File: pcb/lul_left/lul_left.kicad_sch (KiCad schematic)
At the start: 42 parts, among them J1 JST Connector, J2 JST Connector, SW1 SW_Push, SW10 SW_Push, SW11 SW_Push, SW12 SW_Push, SW13 SW_Push, SW14 SW_Push, SW15 SW_Push, SW16 SW_Push, SW17 SW_Push, SW18 SW_Push, SW19 SW_Push, SW2 SW_Push, SW20 SW_Push, SW21 SW_Push, SW22 SW_Push, SW23 SW_Push, SW24 SW_Push, SW25 SW_Push, SW26 SW_Push, SW27 SW_Push, SW28 SW_Push, SW29 SW_Push, SW3 SW_Push, SW30 SW_Push, SW31 SW_Push, SW32 SW_Push, SW33 SW_Push, SW34 SW_Push, SW4 SW_Push, SW5 SW_Push, SW6 SW_Push, SW7 SW_Push, SW8 SW_Push, SW9 SW_Push, U1 nice_nano, U2 nice_nano

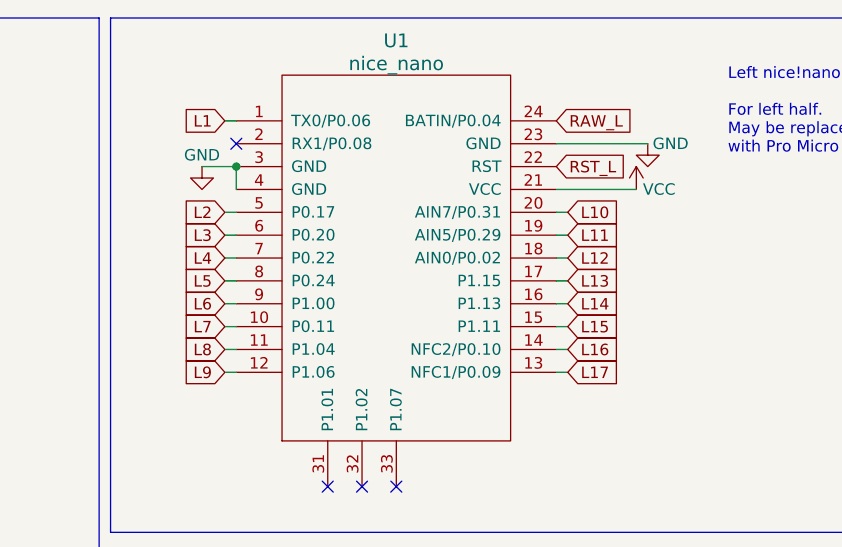
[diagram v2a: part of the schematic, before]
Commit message: route fully. Just need ground fill
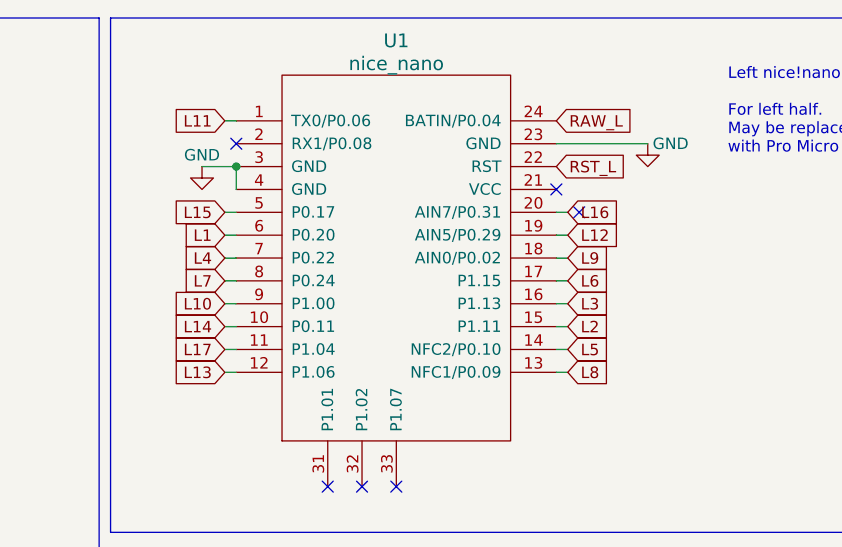
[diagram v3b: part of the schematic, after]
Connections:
- net L1: now also U1.6 (P0.20); no longer U1.1 (TX0/P0.06)
- net L10: now also U1.9 (P1.00); no longer U1.20 (AIN7/P0.31)
- net L11: now also U1.1 (TX0/P0.06); no longer U1.19 (AIN5/P0.29)
- net L12: now also U1.19 (AIN5/P0.29); no longer U1.18 (AIN0/P0.02)
- net L13: now also U1.12 (P1.06); no longer U1.17 (P1.15)
- net L14: now also U1.10 (P0.11); no longer U1.16 (P1.13)
- net L15: now also U1.5 (P0.17); no longer U1.15 (P1.11)
- net L16: now also U1.20 (AIN7/P0.31); no longer U1.14 (NFC2/P0.10)
- net L17: now also U1.11 (P1.04); no longer U1.13 (NFC1/P0.09)
- net L2: now also U1.15 (P1.11); no longer U1.5 (P0.17)
- net L3: now also U1.16 (P1.13); no longer U1.6 (P0.20)
- net L5: now also U1.14 (NFC2/P0.10); no longer U1.8 (P0.24)
- net L6: now also U1.17 (P1.15); no longer U1.9 (P1.00)
- net L7: now also U1.8 (P0.24); no longer U1.10 (P0.11)
- net L8: now also U1.13 (NFC1/P0.09); no longer U1.11 (P1.04)
- net L9: now also U1.18 (AIN0/P0.02); no longer U1.12 (P1.06)
- net VCC: no longer U1.21 (VCC)
- no-connect marks 10 -> 12
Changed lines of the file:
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@@
   (no_connect (at 157.48 64.77))
   (no_connect (at 80.01 171.45))
+  (no_connect (at 181.61 34.29))
   (no_connect (at 161.29 137.16))
   (no_connect (at 157.48 137.16))
   (no_connect (at 161.29 64.77))
+  (no_connect (at 179.07 31.75))
   (no_connect (at 143.51 99.06))
   (wire (pts (xy 62.23 87.63) (xy 62.23 88.9))
@@
   )
   (wire (pts (xy 100.33 67.31) (xy 100.33 68.58))
-    (stroke (width 0) (type default))
-  )
-  (wire (pts (xy 179.07 31.75) (xy 187.96 31.75))
     (stroke (width 0) (type default))
   )
@@
     )
   )
-  (global_label "L6" (shape input) (at 142.24 44.45 180) (fields_autoplaced)
+  (global_label "L10" (shape input) (at 142.24 44.45 180) (fields_autoplaced)
     (effects (font (size 1.27 1.27)) (justify right))
-    (property "Intersheetrefs" "${INTERSHEET_REFS}" (at 137.0966 44.45 0)
+    (property "Intersheetrefs" "${INTERSHEET_REFS}" (at 135.8871 44.45 0)
       (effects (font (size 1.27 1.27)) (justify right) hide)
     )
@@
     )
   )
-  (global_label "L12" (shape input) (at 180.34 39.37 0) (fields_autoplaced)
-    (effects (font (size 1.27 1.27)) (justify left))
-    (property "Intersheetrefs" "${INTERSHEET_REFS}" (at 186.6929 39.37 0)
+  (global_label "L9" (shape input) (at 180.34 39.37 0) (fields_autoplaced)
+    (effects (font (size 1.27 1.27)) (justify left))
+    (property "Intersheetrefs" "${INTERSHEET_REFS}" (at 185.4834 39.37 0)
       (effects (font (size 1.27 1.27)) (justify left) hide)
     )
@@
     )
   )
-  (global_label "L9" (shape input) (at 142.24 52.07 180) (fields_autoplaced)
+  (global_label "L13" (shape input) (at 142.24 52.07 180) (fields_autoplaced)
     (effects (font (size 1.27 1.27)) (justify right))
-    (property "Intersheetrefs" "${INTERSHEET_REFS}" (at 137.0966 52.07 0)
+    (property "Intersheetrefs" "${INTERSHEET_REFS}" (at 135.8871 52.07 0)
       (effects (font (size 1.27 1.27)) (justify right) hide)
     )
@@
     )
   )
-  (global_label "L5" (shape input) (at 142.24 41.91 180) (fields_autoplaced)
+  (global_label "L7" (shape input) (at 142.24 41.91 180) (fields_autoplaced)
     (effects (font (size 1.27 1.27)) (justify right))
     (property "Intersheetrefs" "${INTERSHEET_REFS}" (at 137.0966 41.91 0)
@@
     )
   )
-  (global_label "L16" (shape input) (at 180.34 49.53 0) (fields_autoplaced)
-    (effects (font (size 1.27 1.27)) (justify left))
-    (property "Intersheetrefs" "${INTERSHEET_REFS}" (at 186.6929 49.53 0)
+  (global_label "L5" (shape input) (at 180.34 49.53 0) (fields_autoplaced)
+    (effects (font (size 1.27 1.27)) (justify left))
+    (property "Intersheetrefs" "${INTERSHEET_REFS}" (at 185.4834 49.53 0)
       (effects (font (size 1.27 1.27)) (justify left) hide)
     )
@@
     )
   )
-  (global_label "L15" (shape input) (at 180.34 46.99 0) (fields_autoplaced)
-    (effects (font (size 1.27 1.27)) (justify left))
-    (property "Intersheetrefs" "${INTERSHEET_REFS}" (at 186.6929 46.99 0)
+  (global_label "L2" (shape input) (at 180.34 46.99 0) (fields_autoplaced)
+    (effects (font (size 1.27 1.27)) (justify left))
+    (property "Intersheetrefs" "${INTERSHEET_REFS}" (at 185.4834 46.99 0)
       (effects (font (size 1.27 1.27)) (justify left) hide)
     )
@@
     )
   )
-  (global_label "L14" (shape input) (at 180.34 44.45 0) (fields_autoplaced)
-    (effects (font (size 1.27 1.27)) (justify left))
-    (property "Intersheetrefs" "${INTERSHEET_REFS}" (at 186.6929 44.45 0)
+  (global_label "L3" (shape input) (at 180.34 44.45 0) (fields_autoplaced)
+    (effects (font (size 1.27 1.27)) (justify left))
+    (property "Intersheetrefs" "${INTERSHEET_REFS}" (at 185.4834 44.45 0)
       (effects (font (size 1.27 1.27)) (justify left) hide)
     )
@@
     )
   )
-  (global_label "L3" (shape input) (at 142.24 36.83 180) (fields_autoplaced)
+  (global_label "L1" (shape input) (at 142.24 36.83 180) (fields_autoplaced)
     (effects (font (size 1.27 1.27)) (justify right))
     (property "Intersheetrefs" "${INTERSHEET_REFS}" (at 137.0966 36.83 0)
@@
     )
   )
-  (global_label "L1" (shape input) (at 142.24 24.13 180) (fields_autoplaced)
+  (global_label "L11" (shape input) (at 142.24 24.13 180) (fields_autoplaced)
     (effects (font (size 1.27 1.27)) (justify right))
-    (property "Intersheetrefs" "${INTERSHEET_REFS}" (at 137.0966 24.13 0)
+    (property "Intersheetrefs" "${INTERSHEET_REFS}" (at 135.8871 24.13 0)
       (effects (font (size 1.27 1.27)) (justify right) hide)
     )
   )
-  (global_label "L17" (shape input) (at 180.34 52.07 0) (fields_autoplaced)
-    (effects (font (size 1.27 1.27)) (justify left))
-    (property "Intersheetrefs" "${INTERSHEET_REFS}" (at 186.6929 52.07 0)
+  (global_label "L8" (shape input) (at 180.34 52.07 0) (fields_autoplaced)
+    (effects (font (size 1.27 1.27)) (justify left))
+    (property "Intersheetrefs" "${INTERSHEET_REFS}" (at 185.4834 52.07 0)
       (effects (font (size 1.27 1.27)) (justify left) hide)
     )
@@
     )
   )
-  (global_label "L7" (shape input) (at 142.24 46.99 180) (fields_autoplaced)
+  (global_label "L14" (shape input) (at 142.24 46.99 180) (fields_autoplaced)
     (effects (font (size 1.27 1.27)) (justify right))
-    (property "Intersheetrefs" "${INTERSHEET_REFS}" (at 137.0966 46.99 0)
+    (property "Intersheetrefs" "${INTERSHEET_REFS}" (at 135.8871 46.99 0)
       (effects (font (size 1.27 1.27)) (justify right) hide)
     )
@@
     )
   )
-  (global_label "L2" (shape input) (at 142.24 34.29 180) (fields_autoplaced)
+  (global_label "L15" (shape input) (at 142.24 34.29 180) (fields_autoplaced)
     (effects (font (size 1.27 1.27)) (justify right))
-    (property "Intersheetrefs" "${INTERSHEET_REFS}" (at 137.0966 34.29 0)
+    (property "Intersheetrefs" "${INTERSHEET_REFS}" (at 135.8871 34.29 0)
       (effects (font (size 1.27 1.27)) (justify right) hide)
     )
@@
     )
   )
-  (global_label "L10" (shape input) (at 180.34 34.29 0) (fields_autoplaced)
+  (global_label "L16" (shape input) (at 180.34 34.29 0) (fields_autoplaced)
     (effects (font (size 1.27 1.27)) (justify left))
     (property "Intersheetrefs" "${INTERSHEET_REFS}" (at 186.6929 34.29 0)
@@
     )
   )
-  (global_label "L8" (shape input) (at 142.24 49.53 180) (fields_autoplaced)
+  (global_label "L17" (shape input) (at 142.24 49.53 180) (fields_autoplaced)
     (effects (font (size 1.27 1.27)) (justify right))
-    (property "Intersheetrefs" "${INTERSHEET_REFS}" (at 137.0966 49.53 0)
+    (property "Intersheetrefs" "${INTERSHEET_REFS}" (at 135.8871 49.53 0)
       (effects (font (size 1.27 1.27)) (justify right) hide)
     )
@@
     )
   )
-  (global_label "L13" (shape input) (at 180.34 41.91 0) (fields_autoplaced)
-    (effects (font (size 1.27 1.27)) (justify left))
-    (property "Intersheetrefs" "${INTERSHEET_REFS}" (at 186.6929 41.91 0)
+  (global_label "L6" (shape input) (at 180.34 41.91 0) (fields_autoplaced)
+    (effects (font (size 1.27 1.27)) (justify left))
+    (property "Intersheetrefs" "${INTERSHEET_REFS}" (at 185.4834 41.91 0)
       (effects (font (size 1.27 1.27)) (justify left) hide)
     )
@@
     )
   )
-  (global_label "L11" (shape input) (at 180.34 36.83 0) (fields_autoplaced)
+  (global_label "L12" (shape input) (at 180.34 36.83 0) (fields_autoplaced)
     (effects (font (size 1.27 1.27)) (justify left))
     (property "Intersheetrefs" "${INTERSHEET_REFS}" (at 186.6929 36.83 0)
@@
         )
       )
-    )
-  )
-  (symbol (lib_id "power:VCC") (at 187.96 31.75 0) (unit 1)
-    (in_bom yes) (on_board yes) (dnp no)
-    (property "Reference" "#PWR03" (at 187.96 35.56 0)
-      (effects (font (size 1.27 1.27)) hide)
-    )
-    (property "Value" "VCC" (at 190.5 31.75 0)
-      (effects (font (size 1.27 1.27)))
-    )
-    (property "Footprint" "" (at 187.96 31.75 0)
-      (effects (font (size 1.27 1.27)) hide)
-    )
-    (property "Datasheet" "" (at 187.96 31.75 0)
-      (effects (font (size 1.27 1.27)) hide)
-    )
-    (pin "1")
-    (instances
-      (project "lul_left"
-        (path "/0fb93ee3-bbcd-4139-9e69-991748fbc960"
-          (reference "#PWR03") (unit 1)
-        )
-      )

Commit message: fix small connection issue
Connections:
- net R14: now also U2.7 (P0.22)
- net R16: no longer U2.7 (P0.22)
- net R17: now also U2.8 (P0.24)
- net R6: no longer U2.8 (P0.24)
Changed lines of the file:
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@@
     )
   )
-  (global_label "R16" (shape input) (at 142.24 111.76 180) (fields_autoplaced)
+  (global_label "R14" (shape input) (at 142.24 111.76 180) (fields_autoplaced)
     (effects (font (size 1.27 1.27)) (justify right))
     (property "Intersheetrefs" "${INTERSHEET_REFS}" (at 135.6452 111.76 0)
@@
     )
   )
-  (global_label "R6" (shape input) (at 142.24 114.3 180) (fields_autoplaced)
+  (global_label "R17" (shape input) (at 142.24 114.3 180) (fields_autoplaced)
     (effects (font (size 1.27 1.27)) (justify right))
-    (property "Intersheetrefs" "${INTERSHEET_REFS}" (at 136.8547 114.3 0)
+    (property "Intersheetrefs" "${INTERSHEET_REFS}" (at 135.6452 114.3 0)
       (effects (font (size 1.27 1.27)) (justify right) hide)
     )
